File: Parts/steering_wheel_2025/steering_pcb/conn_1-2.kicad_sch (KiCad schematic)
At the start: 21 parts, among them J1 Button 1 molex-µfit connector, J2 Button 1 molex-µfit connector, Q2 2N7002DW, Q3 2N7002DW, Q5 2N7002DW

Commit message: slight changes in schematic
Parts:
- R11, R16, R18, R19, R22, R24: symbol Device:R -> Device:R_Small
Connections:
- net GND: now also R23.1; no longer R20.2
- net LED_PWM: now also R20.1; no longer R23.2
- net button_2_0: now also R23.2; no longer R20.1
- net at J2.6 (Pin_6): now also R20.2; no longer R23.1
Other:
- moved on the sheet: R20, R23

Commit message: Error fixing with kicad_dru, and silkscreeen updates. TO-DO: BOM to basic
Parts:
- R11, R15, R16, R18, R19, R22, R23, R24: Note (none) -> basic
- R14, R20: JLCPCB (none) -> C25076; Note (none) -> basic
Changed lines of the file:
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@@
 			)
 		)
-		(property "Datasheet" "https://www.lcsc.com/datasheet/lcsc_datasheet_2205311845_UNI-ROYAL-Uniroyal-Elec-0402WGJ0103TCE_C25531.pdf"
+		(property "Datasheet" "https://jlcpcb.com/partdetail/C25531"
 			(at 109.22 39.37 0)
 			(effects
@@
 			)
 		)
-		(property "Description" "Resistor, small symbol"
+		(property "Description" "0402WGJ0103TCE"
 			(at 109.22 39.37 0)
 			(effects
@@
 			)
 		)
+		(property "Note" "basic"
+			(at 109.22 39.37 0)
+			(effects
+				(font
+					(size 1.27 1.27)
+				)
+				(hide yes)
+			)
+		)
 		(pin "1"
 		)
@@
 			)
 		)
-		(property "Datasheet" "~"
+		(property "Datasheet" "https://jlcpcb.com/partdetail/C25531"
 			(at 135.89 68.58 0)
 			(effects
@@
 			)
 		)
-		(property "Description" "Resistor, small symbol"
+		(property "Description" "0402WGJ0103TCE"
 			(at 135.89 68.58 0)
 			(effects
@@
 			)
 		)
+		(property "Note" "basic"
+			(at 135.89 68.58 0)
+			(effects
+				(font
+					(size 1.27 1.27)
+				)
+				(hide yes)
+			)
+		)
 		(pin "1"
 		)
@@
 			)
 		)
-		(property "Datasheet" "~"
+		(property "Datasheet" "https://jlcpcb.com/partdetail/C25531"
 			(at 119.38 68.58 0)
 			(effects
@@
 			)
 		)
-		(property "Description" "Resistor, small symbol"
+		(property "Description" "0402WGJ0103TCE"
 			(at 119.38 68.58 0)
 			(effects
@@
 			)
 		)
+		(property "Note" "basic"
+			(at 119.38 68.58 0)
+			(effects
+				(font
+					(size 1.27 1.27)
+				)
+				(hide yes)
+			)
+		)
 		(pin "1"
 		)
@@
 			)
 		)
-		(property "Datasheet" "~"
+		(property "Datasheet" "https://jlcpcb.com/partdetail/C25531"
 			(at 158.75 68.58 0)
 			(effects
@@
 			)
 		)
-		(property "Description" "Resistor, small symbol"
+		(property "Description" "0402WGJ0103TCE"
 			(at 158.75 68.58 0)
 			(effects
@@
 			)
 		)
+		(property "Note" "basic"
+			(at 158.75 68.58 0)
+			(effects
+				(font
+					(size 1.27 1.27)
+				)
+				(hide yes)
+			)
+		)
 		(pin "1"
 		)
@@
 			)
 		)
-		(property "Datasheet" "~"
+		(property "Datasheet" "https://jlcpcb.com/partdetail/C25531"
 			(at 191.77 68.58 0)
 			(effects
@@
 			)
 		)
-		(property "Description" "Resistor, small symbol"
+		(property "Description" "0402WGJ0103TCE"
 			(at 191.77 68.58 0)
 			(effects
@@
 			)
 		)
+		(property "Note" "basic"
+			(at 191.77 68.58 0)
+			(effects
+				(font
+					(size 1.27 1.27)
+				)
+				(hide yes)
+			)
+		)
 		(pin "1"
 		)
@@
 			)
 		)
-		(property "Datasheet" "~"
+		(property "Datasheet" "https://jlcpcb.com/partdetail/C25531"
 			(at 102.87 68.58 0)
 			(effects
@@
 			)
 		)
-		(property "Description" "Resistor, small symbol"
+		(property "Description" "0402WGJ0103TCE"
 			(at 102.87 68.58 0)
 			(effects
@@
 			)
 		)
+		(property "Note" "basic"
+			(at 102.87 68.58 0)
+			(effects
+				(font
+					(size 1.27 1.27)
+				)
+				(hide yes)
+			)
+		)
 		(pin "1"
 		)
@@
 			)
 		)
-		(property "Datasheet" "~"
+		(property "Datasheet" "https://jlcpcb.com/partdetail/C25531"
 			(at 175.26 68.58 0)
 			(effects
@@
 			)
 		)
-		(property "Description" "Resistor, small symbol"
+		(property "Description" "0402WGJ0103TCE"
 			(at 175.26 68.58 0)
 			(effects
@@
 			)
 		)
+		(property "Note" "basic"
+			(at 175.26 68.58 0)
+			(effects
+				(font
+					(size 1.27 1.27)
+				)
+				(hide yes)
+			)
+		)
 		(pin "1"
 		)
@@
 			)
 		)
-		(property "Datasheet" ""
+		(property "Datasheet" "https://jlcpcb.com/partdetail/25819-0402WGF1000TCE/C25076"
 			(at 176.53 39.37 0)
 			(effects
@@
 			)
 		)
-		(property "Description" "100"
+		(property "Description" "0402WGF1000TCE"
 			(at 176.53 39.37 0)
 			(effects
@@
 			)
 		)
-		(property "JLCPCB" ""
+		(property "JLCPCB" "C25076"
 			(at 176.53 39.37 0)
 			(effects
@@
 			)
 		)
+		(property "Note" "basic"
+			(at 176.53 39.37 0)
+			(effects
+				(font
+					(size 1.27 1.27)
+				)
+				(hide yes)
+			)
+		)
 		(pin "1"
 		)
@@
 			)
 		)
-		(property "Datasheet" ""
+		(property "Datasheet" "https://jlcpcb.com/partdetail/25819-0402WGF1000TCE/C25076"
 			(at 120.65 39.37 0)
 			(effects
@@
 			)
 		)
-		(property "Description" "100"
+		(property "Description" "0402WGF1000TCE"
 			(at 120.65 39.37 0)
 			(effects
@@
 			)
 		)
-		(property "JLCPCB" ""
+		(property "JLCPCB" "C25076"
 			(at 120.65 39.37 0)
 			(effects
@@
 			)
 		)
+		(property "Note" "basic"
+			(at 120.65 39.37 0)
+			(effects
+				(font
+					(size 1.27 1.27)
+				)
+				(hide yes)
+			)
+		)
 		(pin "1"
 		)
@@
 			)
 		)
-		(property "Datasheet" "https://www.lcsc.com/datasheet/lcsc_datasheet_2205311845_UNI-ROYAL-Uniroyal-Elec-0402WGJ0103TCE_C25531.pdf"
+		(property "Datasheet" "https://jlcpcb.com/partdetail/C25531"
 			(at 165.1 39.37 0)
 			(effects
@@
 			)
 		)
-		(property "Description" "Resistor, small symbol"
+		(property "Description" "0402WGJ0103TCE"
 			(at 165.1 39.37 0)
 			(effects
@@
 			(at 165.1 39.37 0)
 			(effects
+				(font
+					(size 1.27 1.27)
+				)
+				(hide yes)
+			)
+		)
+		(property "Note" "basic"
+			(at 165.1 39.37 0)
+			(effects

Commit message: board update
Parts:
- D1, D2: value BAS16VYs -> ~; Note (none) -> no; Product (none) -> BAS16VYs
- DZ1, DZ2: Note (none) -> no; Product (none) -> BZX84C3V3TS-7-F
- Q2, Q3, Q5: Note (none) -> no; Product (none) -> 2N7002DW
- R11, R15, R16, R18, R19, R22, R23, R24: Product (none) -> 0402WGJ0103TCE
- R14, R20: Product (none) -> 0402WGF1000TCE
- R17, R21: value 180 -> 100; JLCPCB C38941 -> C25076; Note (none) -> basic; Product (none) -> 0402WGF1000TCE

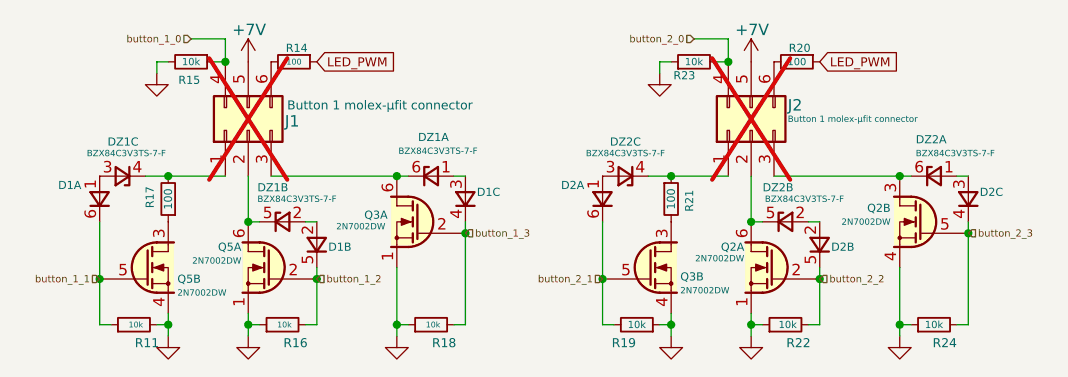
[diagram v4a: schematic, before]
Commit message: Rename folders for consistency
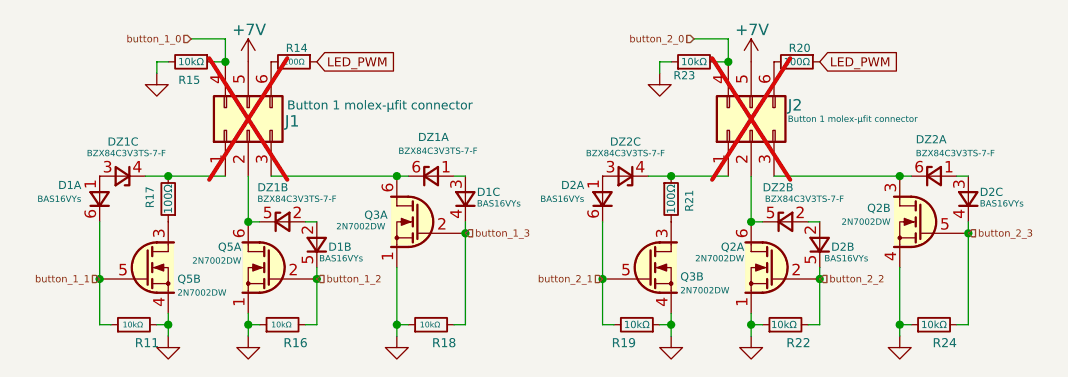
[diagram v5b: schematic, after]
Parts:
- D1, D2: value ~ -> BAS16VYs
- R11, R15, R16, R18, R19, R22, R23, R24: value 10k -> 10kΩ
- R14, R17, R20, R21: value 100 -> 100Ω
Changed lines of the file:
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@@
 (kicad_sch
-	(version 20231120)
+	(version 20250114)
 	(generator "eeschema")
-	(generator_version "8.0")
+	(generator_version "9.0")
 	(paper "A4")
 	(junction
@@
 			)
 		)
-		(property "Value" "~"
+		(property "Value" "BAS16VYs"
 			(at 196.85 55.118 90)
 			(effects
@@
 			)
 		)
-		(property "Value" "~"
+		(property "Value" "BAS16VYs"
 			(at 140.97 55.118 90)
 			(effects
@@
 			)
 		)
-		(property "Value" "100"
+		(property "Value" "100Ω"
 			(at 106.68 54.61 90)
 			(effects
@@
 			)
 		)
-		(property "Value" "10k"
+		(property "Value" "10kΩ"
 			(at 109.22 39.37 90)
 			(effects
@@
 			)
 		)
-		(property "Value" "10k"
+		(property "Value" "10kΩ"
 			(at 136.906 68.58 90)
 			(effects
@@
 			)
 		)
-		(property "Value" "10k"
+		(property "Value" "10kΩ"
 			(at 120.396 68.58 90)
 			(effects
@@
 			)
 		)
-		(property "Value" "10k"
+		(property "Value" "10kΩ"
 			(at 158.75 68.58 90)
 			(effects
@@
 			)
 		)
-		(property "Value" "~"
+		(property "Value" "BAS16VYs"
 			(at 152.908 54.61 90)
 			(effects
@@
 			)
 		)
-		(property "Value" "~"
+		(property "Value" "BAS16VYs"
 			(at 123.444 61.214 90)
 			(effects
@@
 			)
 		)
-		(property "Value" "~"
+		(property "Value" "BAS16VYs"
 			(at 97.028 54.61 90)
 			(effects
@@
 			)
 		)
-		(property "Value" "10k"
+		(property "Value" "10kΩ"
 			(at 191.77 68.58 90)
 			(effects
@@
 			)
 		)
-		(property "Value" "10k"
+		(property "Value" "10kΩ"
 			(at 103.886 68.58 90)
 			(effects
@@
 			)
 		)
-		(property "Value" "10k"
+		(property "Value" "10kΩ"
 			(at 176.53 68.58 90)
 			(effects
@@
 			)
 		)
-		(property "Value" "100"
+		(property "Value" "100Ω"
 			(at 176.53 39.37 90)
 			(effects
@@
 			)
 		)
-		(property "Value" "100"
+		(property "Value" "100Ω"
 			(at 120.65 39.37 90)
 			(effects
@@
 			)
 		)
-		(property "Value" "10k"
+		(property "Value" "10kΩ"
 			(at 165.1 39.37 90)
 			(effects
@@
 			)
 		)
-		(property "Value" "100"
+		(property "Value" "100Ω"
 			(at 162.56 54.61 90)
 			(effects
@@
 			)
 		)
-		(property "Value" "~"
+		(property "Value" "BAS16VYs"
 			(at 179.578 61.214 90)
 			(effects
